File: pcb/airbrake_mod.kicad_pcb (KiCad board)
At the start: 4 copper layers, 65.7 x 107.9 mm, 134 parts, among them J1 XT30PW-M, J2 Same Sky UJ20-C-H-G-SMT-P16-TR, J3 0436500315, J5 CNC_Tech_3220-14-0100-00, Q1 NTR4003N, Q2 NTR4003N, Q3 Si3407DV, Q4 NTR4003N, Q5 Si3407DV, Q6 NTR4003N, SW1 GSPTS0018, SW2 GSPTS0018, SW4 GSPTS0018, SW5 GSPTS0018, SW6 GSPTS0018, SW7 GSPTS0018, U1 STM32H730VBTx, U2 TPS561246DRLR, U3 ZXCT180A4W5, U4 USBLC6-2SC6, U5 W25Q128JVS, U6 LPS22DF, U7 LSM6DSV80X, U8 IIS2MDC, Y1 ECS-160-12-33B2Q-JES-TR3

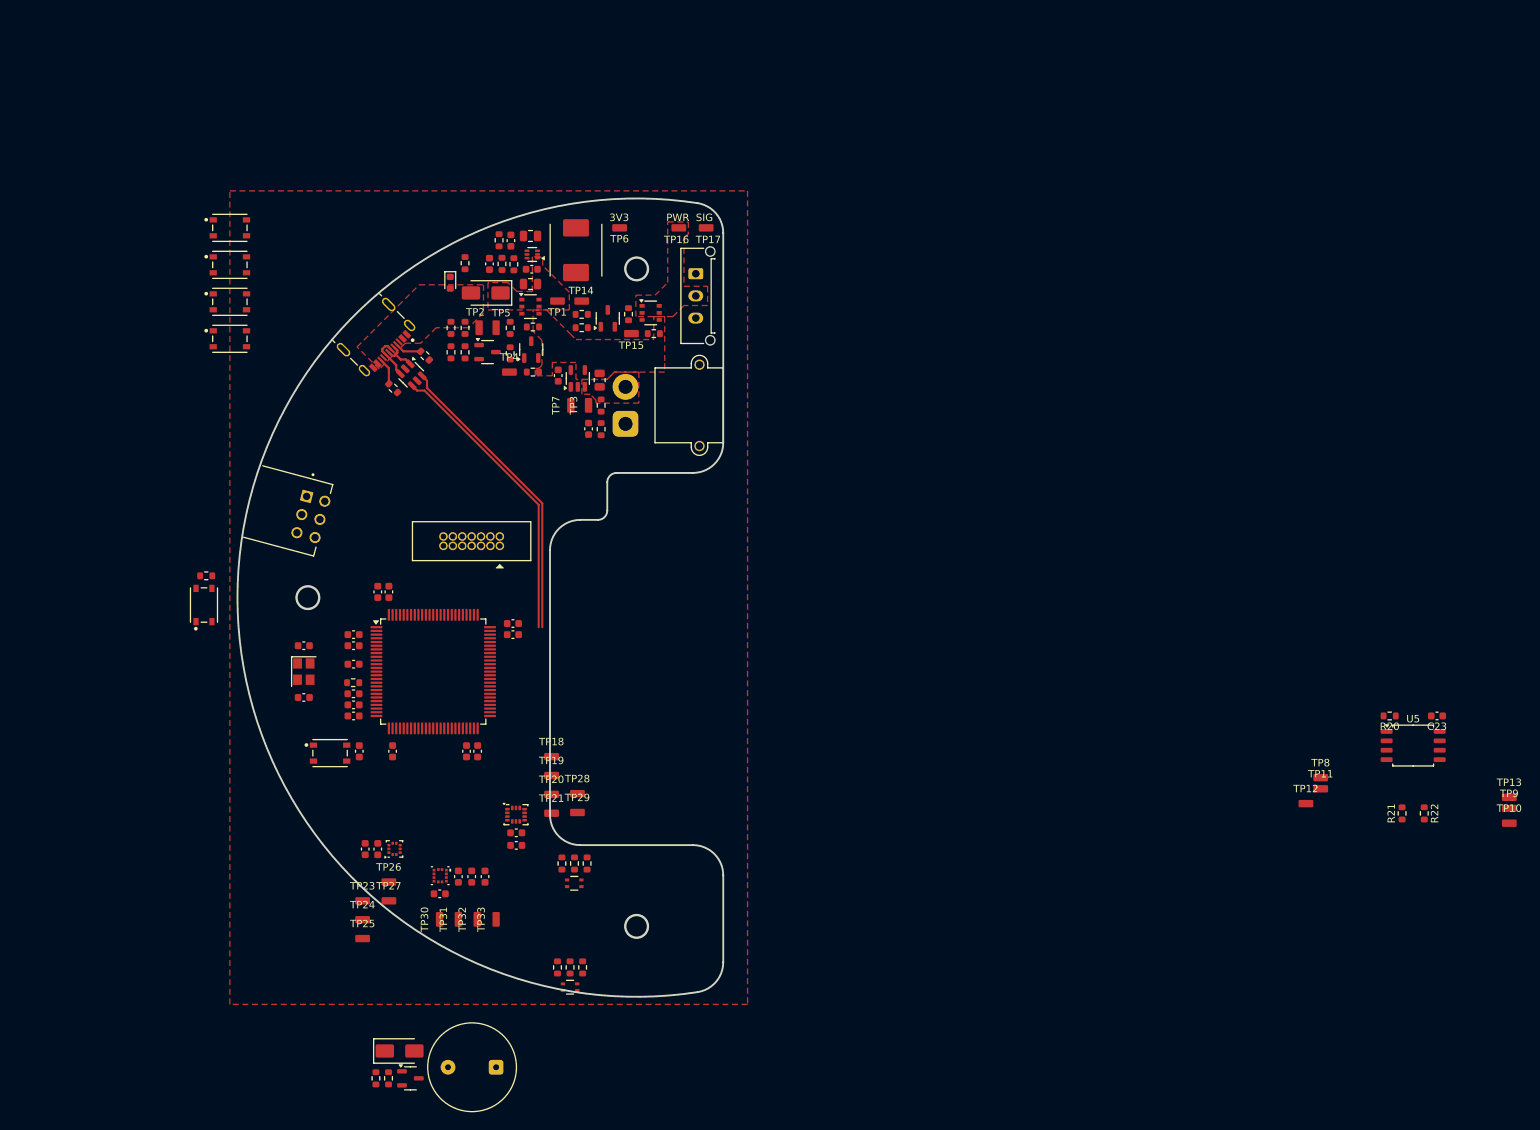
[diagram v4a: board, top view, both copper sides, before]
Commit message: Finish routing with rotated STM32
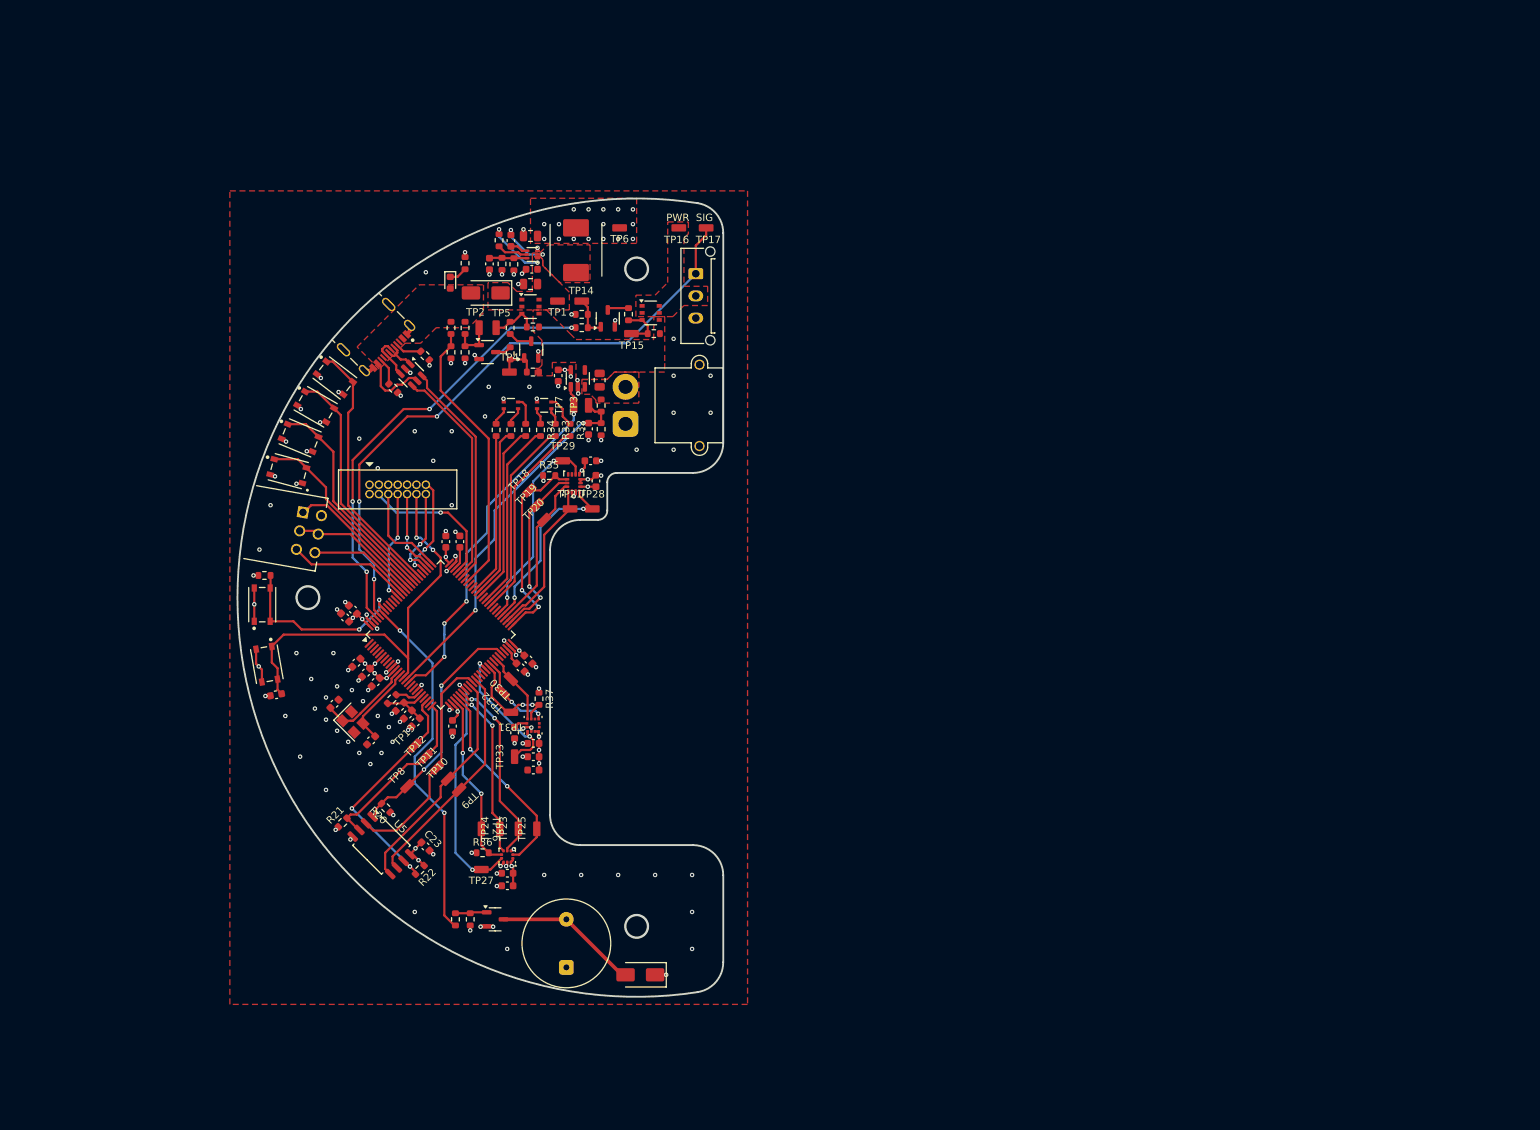
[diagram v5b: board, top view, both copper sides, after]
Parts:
- added R35: 47k, Resistor_SMD:R_0603_1608Metric, F.Cu at (88.2, 83.5)
- added R36: 47k, Resistor_SMD:R_0603_1608Metric, F.Cu at (79.2, 134.5)
- added R37: 47k, Resistor_SMD:R_0603_1608Metric, F.Cu at (86.8, 113.7)
- R27, R32: value 430 -> 150
- R29, R31, R33, R34: value 330 -> 50
- moved TP13 148.2 mm to (70.0, 120.0), turned to 45 degrees
- moved TP10 143.6 mm to (74.5, 124.5), turned to 45 degrees
- moved R21 143.3 mm to (60.2, 130.4), turned to 45 degrees
- moved TP9 142.0 mm to (76.0, 126.0), turned to -135 degrees
- moved U5 140.2 mm to (65.5, 133.5), turned to -45 degrees
- moved C23 137.9 mm to (71.4, 133.6), turned to -45 degrees
- moved R20 136.3 mm to (66.1, 128.4), turned to 135 degrees
- moved R22 136.0 mm to (70.7, 136.8), turned to -135 degrees
- moved TP8 123.5 mm to (69.0, 125.5), turned to 45 degrees
- moved TP11 119.5 mm to (73.0, 123.0), turned to 45 degrees
- moved TP12 119.2 mm to (71.5, 121.5), turned to 45 degrees
- moved D5 78.8 mm to (87.5, 74.0), turned to 180 degrees
- moved R34 72.9 mm to (87.0, 77.3), turned to -90 degrees
- moved R33 72.7 mm to (89.0, 77.3), turned to -90 degrees
- moved R32 72.7 mm to (91.0, 77.3), turned to -90 degrees
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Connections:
- D3 pad 4: +BATT -> +3V3
- D5 pad 4: +BATT -> +3V3
- U1 pad 85: /MCU/MODE_C -> /MCU/MODE_1
- U1 pad 86: /MCU/MODE_1 -> /MCU/MODE_C
- U1 pad 92: /MCU/I2C1_SCL -> unconnected-(U1-PB6-Pad92)
- U1 pad 93: /MCU/I2C1_SDA -> unconnected-(U1-PB7-Pad93)
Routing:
- net /MCU/SERVO_SIG: track 0.00 -> 84.5 mm, vias 0 -> 3
- net /MCU/SERVO_EN: track 0.00 -> 60.3 mm, vias 0 -> 4
- net +3V3: track 0.00 -> 59.4 mm, vias 0 -> 55
- net /Debug/~{RESET}: track 0.00 -> 56.0 mm, vias 0 -> 2
- net GND: track 0.00 -> 55.9 mm, vias 0 -> 112
- net /MCU/BATT_VSENSE: track 0.00 -> 50.8 mm, vias 0 -> 2
- net /MCU/BATT_ISENSE: track 0.00 -> 50.2 mm, vias 0 -> 4
- net /MCU/BUZZER: track 0.00 -> 48.5 mm, vias 0 -> 2
- net /MCU/USB_VBUS_SENSE: track 0.00 -> 37.9 mm
- net /MCU/BTN_0: track 0.00 -> 35.2 mm
- net /Flash/IO3: track 0.00 -> 33.0 mm, vias 0 -> 2
- net /Flash/~{CS}: track 0.00 -> 32.7 mm, vias 0 -> 2
- net /MCU/BARO_INT: track 0.00 -> 32.6 mm, vias 0 -> 2
- net /MCU/BTN_1: track 0.00 -> 32.5 mm
- net /Flash/IO0: track 0.00 -> 31.4 mm
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- added copper zone on F.Cu, net +3V3
- added copper zone on F.Cu, net Net-(U2-SW)
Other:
- board text removed: "3V3"

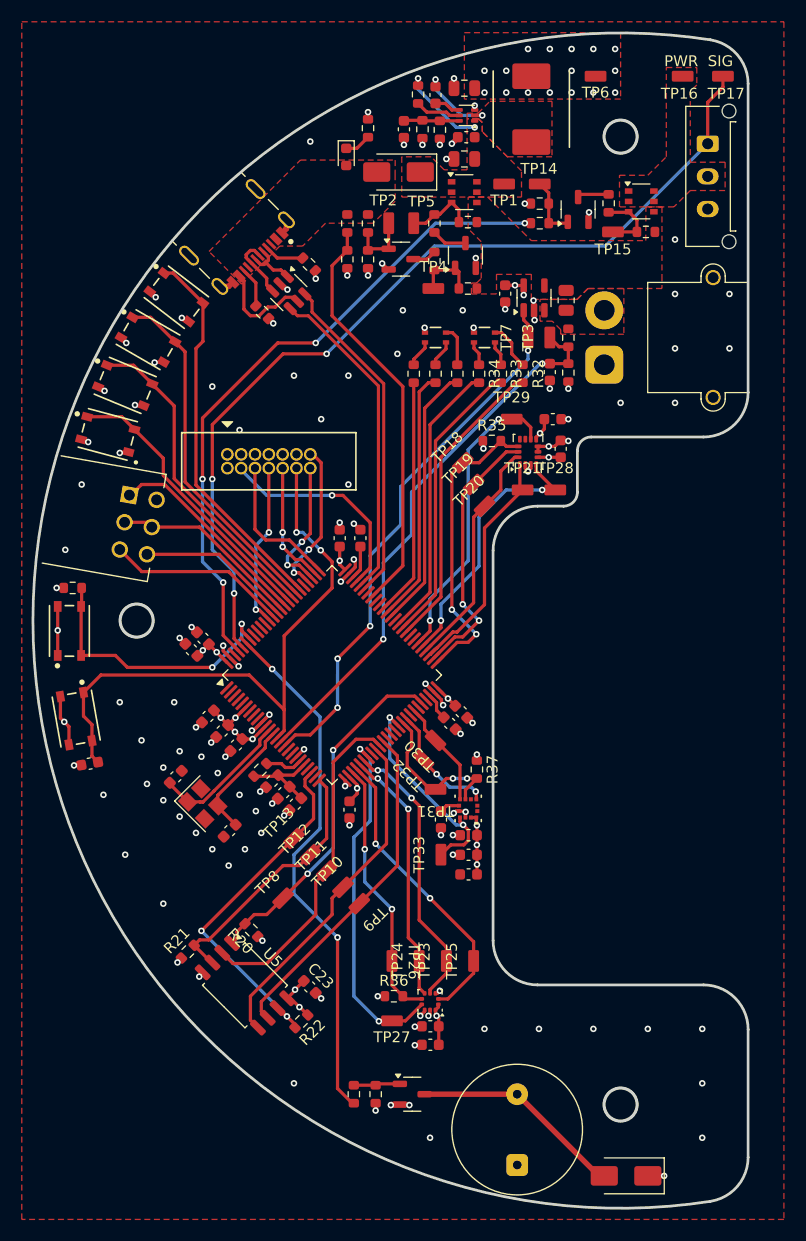
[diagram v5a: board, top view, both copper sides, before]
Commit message: Incorporate feedback servo with 4 pin molex and additional ADC channel
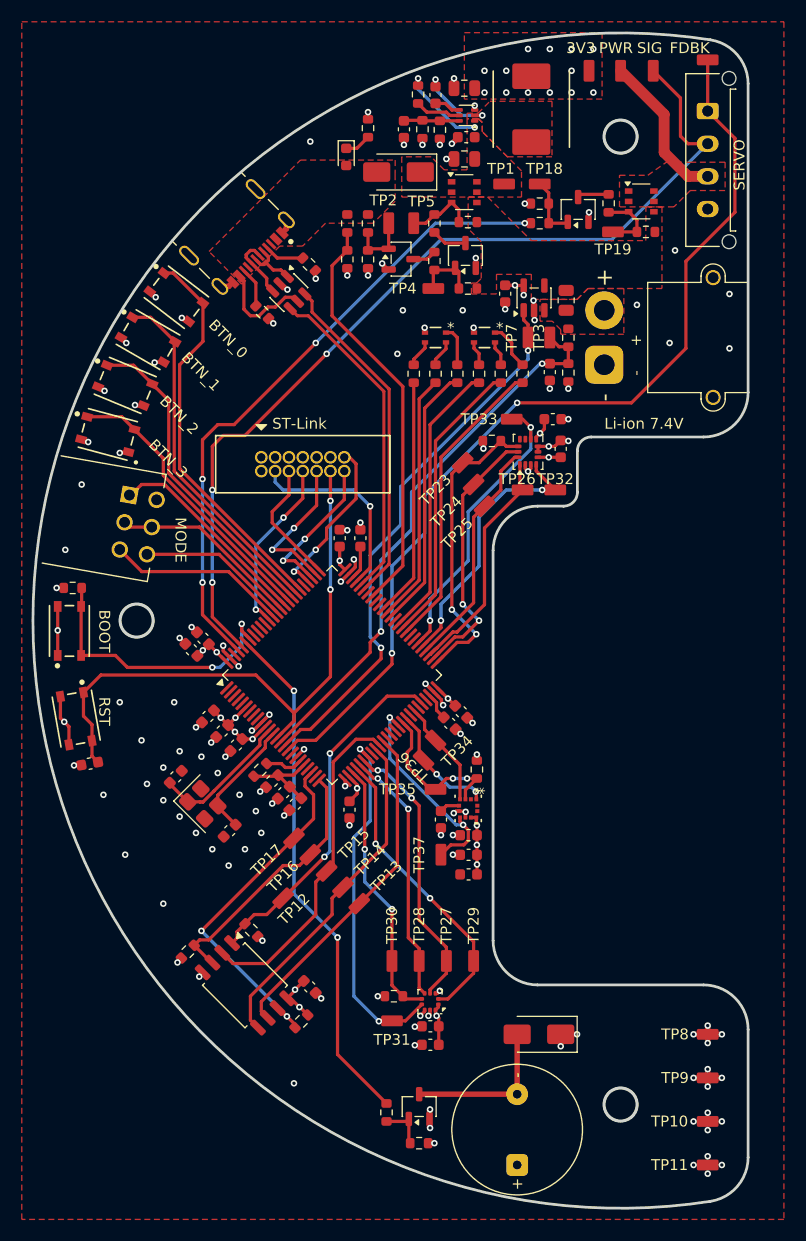
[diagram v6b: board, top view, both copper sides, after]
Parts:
- added TP10: RCUCTE, TestPoint_KOASpeer:TestPoint_Chip_RCUCTE_0603, F.Cu at (108.0, 146.0)
- added TP11: RCUCTE, TestPoint_KOASpeer:TestPoint_Chip_RCUCTE_0603, F.Cu at (108.0, 150.0)
- added TP22: RCUCTE, TestPoint_KOASpeer:TestPoint_Chip_RCUCTE_0603, F.Cu at (108.0, 48.5)
- added TP8: RCUCTE, TestPoint_KOASpeer:TestPoint_Chip_RCUCTE_0603, F.Cu at (108.0, 138.0)
- added TP9: RCUCTE, TestPoint_KOASpeer:TestPoint_Chip_RCUCTE_0603, F.Cu at (108.0, 142.0)
- J3: value 0436500315 -> 0436500415; footprint Connector_Molex:Molex_Micro-Fit_3.0_43650-0315_1x03_P3.00mm_Vertical -> Connector_Molex:Molex_Micro-Fit_3.0_43650-0415_1x04_P3.00mm_Vertical
- moved D4 15.3 mm to (92.5, 138.0)
- moved TP21 6.42 mm to (103.0, 49.5), turned to 90 degrees
- moved R30 6.02 mm to (81.5, 148.0), turned to 0 degrees
- moved TP20 5.72 mm to (100.0, 49.5), turned to 90 degrees
- moved R28 3.44 mm to (78.5, 145.2), turned to -90 degrees
- moved J6 3.13 mm to (67.0, 85.0)
- moved J3 3.00 mm to (108.0, 53.2)
- moved Q6 1.30 mm to (81.5, 144.6), turned to 90 degrees
- moved TP6 0.78 mm to (97.1, 49.5), turned to 90 degrees
- renumbered J5 to J6, TP8 to TP12, TP9 to TP13, TP10 to TP14, TP11 to TP15, TP12 to TP16, TP13 to TP17, TP14 to TP18, TP15 to TP19, TP16 to TP20, TP17 to TP21, TP18 to TP23, TP19 to TP24, TP20 to TP25, TP21 to TP26, TP23 to TP27, TP24 to TP28, TP25 to TP29, TP26 to TP30, TP27 to TP31, TP28 to TP32, TP29 to TP33, TP30 to TP34, TP31 to TP35, TP32 to TP36, TP33 to TP37
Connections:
- J3 pad 1: /MCU/SERVO_SIG -> /MCU/SERVO_FDBK
- J3 pad 2: /Servo/SERVO_PWR -> /MCU/SERVO_SIG
- J3 pad 3: GND -> /Servo/SERVO_PWR
- U1 pad 17: unconnected-(U1-PC2_C-Pad17) -> /MCU/SERVO_FDBK
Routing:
- net /MCU/SERVO_FDBK: track 0.00 -> 88.5 mm, vias 0 -> 2
- net /Servo/SERVO_PWR: track 0.00 -> 14.1 mm
- net +3V3: track 59.4 -> 68.9 mm, vias 55 -> 61
- net Net-(BZ1--): track 19.6 -> 14.5 mm
- net /Debug/JTDI: track 11.2 -> 13.8 mm
- net /MCU/SERVO_SIG: track 84.5 -> 86.4 mm
- net /Debug/JTMS: track 19.9 -> 18.1 mm
- net /Debug/JCLK: track 13.1 -> 11.5 mm
- net /Debug/VCP_TX: track 12.4 -> 13.8 mm
- net /MCU/BTN_0: track 35.2 -> 36.4 mm
- net /Debug/VCP_RX: track 14.0 -> 15.2 mm
- net /MCU/SERVO_EN: track 60.3 -> 59.1 mm
- net /Debug/~{RESET}: track 56.0 -> 54.9 mm
- net /Debug/JTDO: track 15.1 -> 16.1 mm
- net /MCU/BUZZER: track 48.5 -> 47.6 mm
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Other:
- board text added: "- +"
- board text added: "3V3"
- board text added: "BOOT"
- board text added: "BTN_0"
- board text added: "BTN_1"
- board text added: "BTN_2"
- board text added: "BTN_3"
- board text added: "FDBK"
- board text added: "Li-ion 7.4V"
- board text added: "MODE"
- board text added: "RST"
- board text added: "SERVO"
- board text added: "ST-Link"
